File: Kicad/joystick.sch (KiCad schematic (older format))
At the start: 1 part, among them J1101 DE9 Male

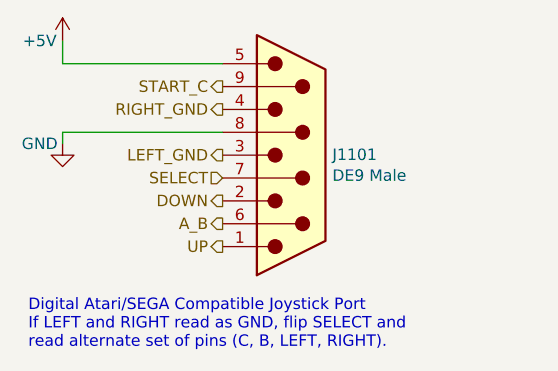
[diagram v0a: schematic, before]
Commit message: Working on layout.
Laid out the parallel port - reordered some pins to make it easier.
Set the minimum track widths to 6 mil/6 mil with a 6mm/3mm via.
Replaced the SPST power switch with a PUE to match the reset switch.
Attached some existing 3D models to the PCB footprints.
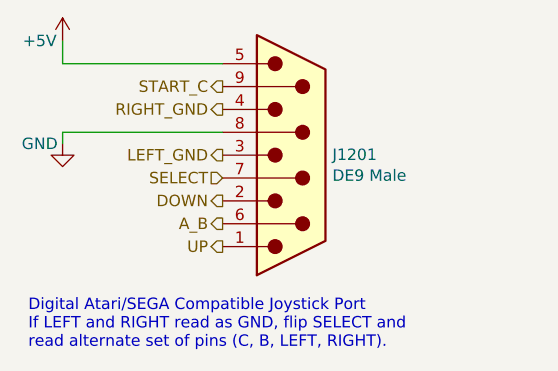
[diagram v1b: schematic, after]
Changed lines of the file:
@@
 AR Path="/5DF2662E/5F3EF2EB/5F3EBC7F" Ref="J?"  Part="1"
 AR Path="/5DF2662E/5F80F300/5F3EBC7F" Ref="J1201"  Part="1"
-F 0 "J1101" H 6530 3652 50  0000 L CNN
+F 0 "J1201" H 6530 3652 50  0000 L CNN
 F 1 "DE9 Male" H 6530 3561 50  0000 L CNN
 F 2 "Connector_Dsub:DSUB-9_Male_Horizontal_P2.77x2.84mm_EdgePinOffset14.56mm_Housed_MountingHolesOffset8.20mm" H 6350 3650 50  0001 C CNN

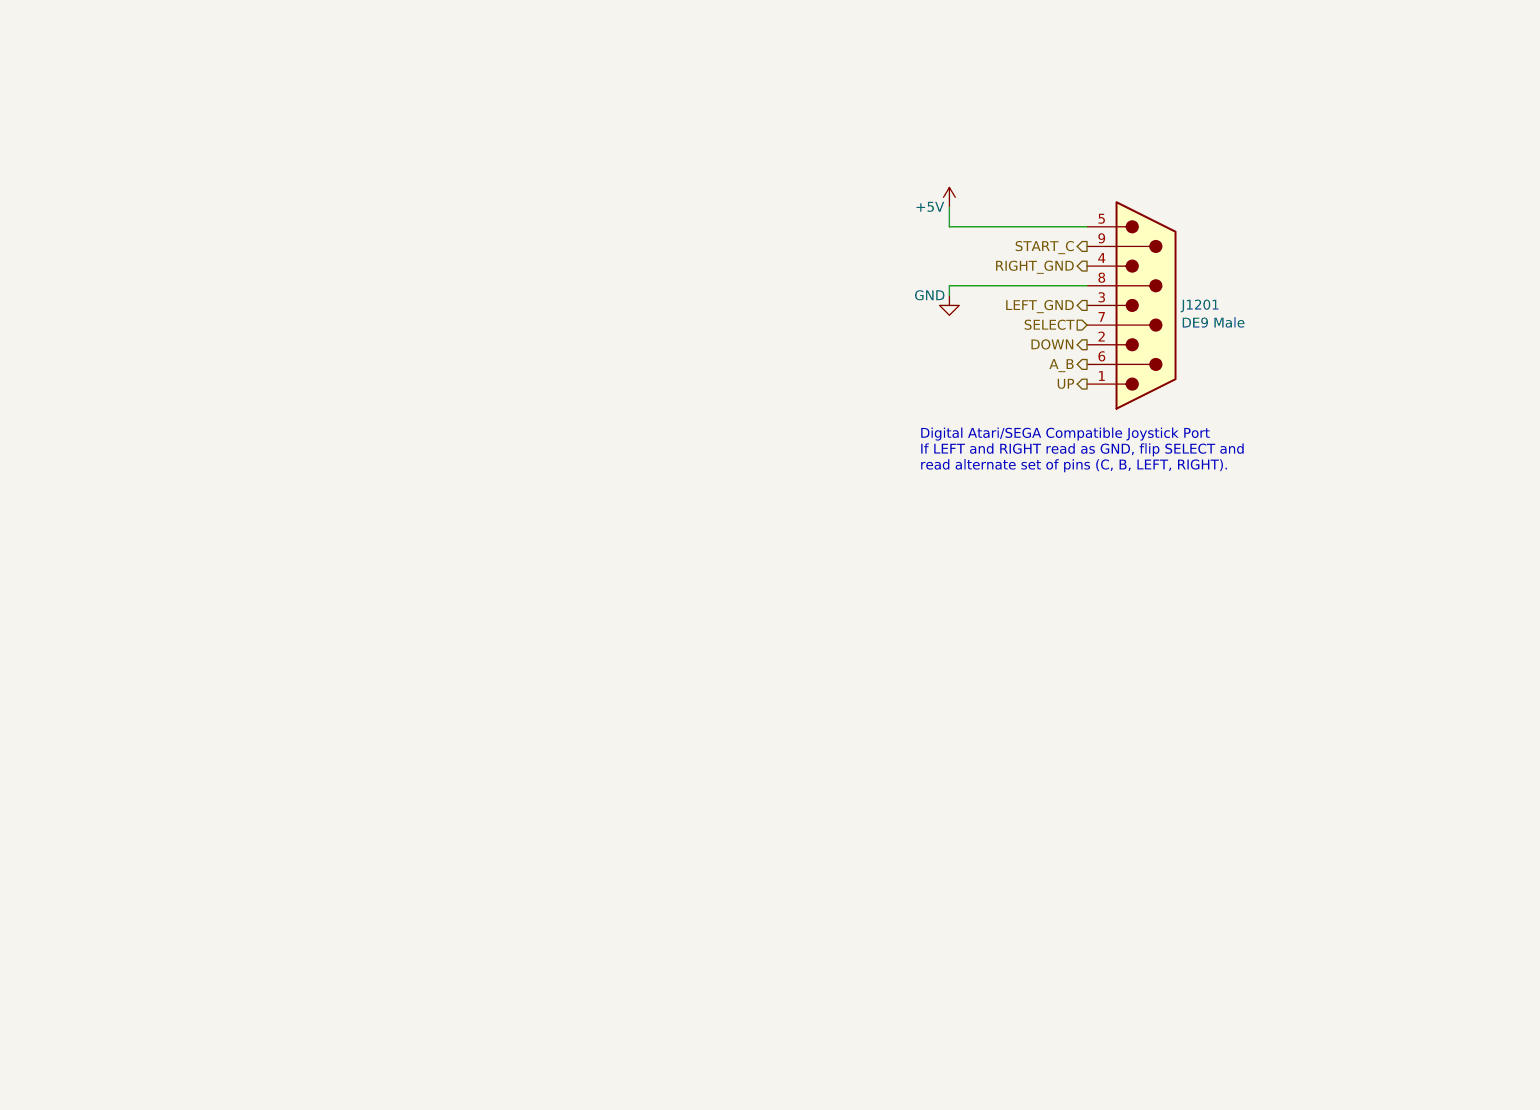
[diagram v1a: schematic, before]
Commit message: Moved Joystick controller onto its own sheet.
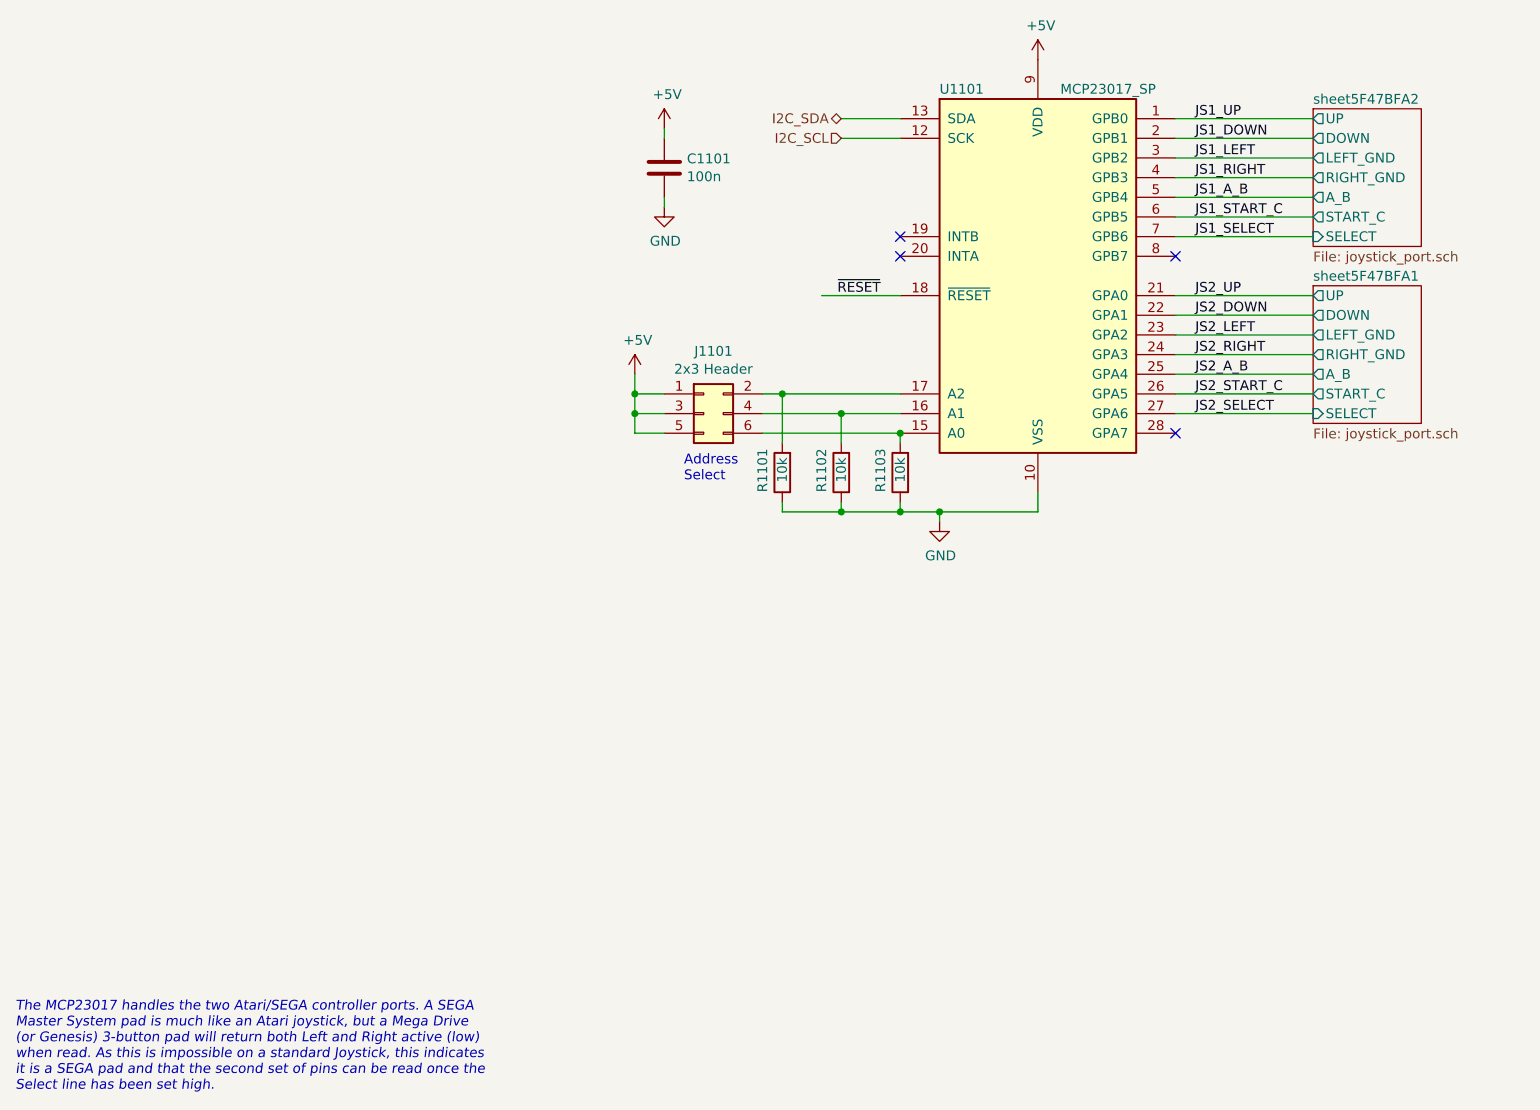
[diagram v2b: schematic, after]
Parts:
- removed J1101: DE9 Male, Connector_Dsub:DSUB-9_Male_Horizontal_P2.77x2.84mm_EdgePinOffset14.56mm_Housed_MountingHolesOffset8.20mm, symbol Connector:DB9_Male
- added C1101: 100n, Capacitor_THT:C_Disc_D3.0mm_W2.0mm_P2.50mm, symbol Device:C
- added J1101: 2x3 Header, Connector_PinHeader_2.54mm:PinHeader_2x03_P2.54mm_Vertical, symbol Connector_Generic:Conn_02x03_Odd_Even
- added R1101, R1102, R1103: 10k, Resistor_THT:R_Axial_DIN0207_L6.3mm_D2.5mm_P10.16mm_Horizontal, symbol Device:R
- added U1101: MCP23017_SP, Package_DIP:DIP-28_W7.62mm, symbol Interface_Expansion:MCP23017_SP
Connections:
- net +5V: now also C1101.1, J1101.1 (Pin_1), J1101.3 (Pin_3), J1101.5 (Pin_5), U1101.9 (VDD)
- net GND: now also C1101.2, R1101.1, R1102.1, R1103.1, U1101.10 (VSS)
- new net: J1101.2 (Pin_2), R1101.2, U1101.17 (A2)
- new net: J1101.4 (Pin_4), R1102.2, U1101.16 (A1)
- new net: J1101.6 (Pin_6), R1103.2, U1101.15 (A0)
- new net I2C_SCL: U1101.12 (SCK)
- new net I2C_SDA: U1101.13 (SDA)
- new net JS1_A_B: U1101.5 (GPB4)
- new net JS1_DOWN: U1101.2 (GPB1)
- new net JS1_LEFT: U1101.3 (GPB2)
- new net JS1_RIGHT: U1101.4 (GPB3)
- new net JS1_SELECT: U1101.7 (GPB6)
- new net JS1_START_C: U1101.6 (GPB5)
- new net JS1_UP: U1101.1 (GPB0)
- new net JS2_A_B: U1101.25 (GPA4)
- new net JS2_DOWN: U1101.22 (GPA1)
- new net JS2_LEFT: U1101.23 (GPA2)
- new net JS2_RIGHT: U1101.24 (GPA3)
- new net JS2_SELECT: U1101.27 (GPA6)
- new net JS2_START_C: U1101.26 (GPA5)
- new net JS2_UP: U1101.21 (GPA0)
- new net ~RESET: U1101.18 (~RESET~)
- no-connect marks 0 -> 4
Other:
- note added: "Address\nSelect"
- note added: "The MCP23017 handles the two Atari/SEGA controller ports. A SEGA\nMaster System pad is much like an Atari joystick, but a Mega Drive\n(or Genesis) 3-button pad will return both Left and Right active (low)\nwhen read. As this is impossible on a standard Joystick, this indicates\nit is a SEGA pad and that the second set of pins can be read once the\nSelect line has been set high."
- note removed: "Digital Atari/SEGA Compatible Joystick Port\nIf LEFT and RIGHT read as GND, flip SELECT and\nread alternate set of pins (C, B, LEFT, RIGHT)."
